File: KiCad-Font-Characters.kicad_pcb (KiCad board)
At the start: 2 copper layers, 296 x 287 mm, 0 parts

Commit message: Modified layout to one column and updated with Greek/Coptic and Cyrillic pages
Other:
- board size 296 x 287 mm -> 147 x 801 mm
- board text added: "KiCad Font - Unicode Pages not implemented are omitted"
- board text removed: "KiCad Font"
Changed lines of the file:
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@@
     (thickness 1.6)
   )
-  (paper "User" 315.011 315.011)
+  (paper "User" 167.005 821.004)
   (title_block
     (title "KiCad Font Characters")
@@
     )
     (pad_to_mask_clearance 0)
-    (grid_origin 13 14)
     (pcbplotparams
       (layerselection 0x0000020_7ffffffe)
@@
   )
   (net 0 "")
-  (gr_line (start 176 82) (end 176 136)
-    (stroke (width 0.15) (type default)) (layer "F.SilkS"))
-  (gr_line (start 176 150) (end 176 172)
-    (stroke (width 0.15) (type default)) (layer "F.SilkS"))
-  (gr_line (start 303 86) (end 162 86)
+  (gr_line (start 27 596) (end 27 650)
+    (stroke (width 0.15) (type default)) (layer "F.SilkS"))
+  (gr_line (start 27 664) (end 27 686)
+    (stroke (width 0.15) (type default)) (layer "F.SilkS"))
+  (gr_line (start 154 600) (end 13 600)
     (stroke (width 0.15) (type default)) (layer "F.SilkS"))
   (gr_line (start 27 139) (end 27 193)
     (stroke (width 0.15) (type default)) (layer "F.SilkS"))
-  (gr_line (start 162 31) (end 303 31)
-    (stroke (width 0.15) (type default)) (layer "F.SilkS"))
-  (gr_line (start 176 27) (end 176 68)
+  (gr_line (start 13 443) (end 154 443)
+    (stroke (width 0.15) (type default)) (layer "F.SilkS"))
+  (gr_line (start 13 313) (end 154 313)
+    (stroke (width 0.15) (type default)) (layer "F.SilkS"))
+  (gr_line (start 27 309) (end 27 350)
+    (stroke (width 0.15) (type default)) (layer "F.SilkS"))
+  (gr_line (start 13 564) (end 154 564)
     (stroke (width 0.15) (type default)) (layer "F.SilkS"))
   (gr_line (start 13 143) (end 154 143)
@@
   (gr_line (start 13 87) (end 154 87)
     (stroke (width 0.15) (type default)) (layer "F.SilkS"))
-  (gr_line (start 176 186) (end 176 285)
+  (gr_line (start 27 700) (end 27 799)
     (stroke (width 0.15) (type default)) (layer "F.SilkS"))
   (gr_line (start 27 27) (end 27 68)
     (stroke (width 0.15) (type default)) (layer "F.SilkS"))
-  (gr_line (start 303 154) (end 162 154)
+  (gr_line (start 27 560) (end 27 582)
+    (stroke (width 0.15) (type default)) (layer "F.SilkS"))
+  (gr_line (start 154 668) (end 13 668)
+    (stroke (width 0.15) (type default)) (layer "F.SilkS"))
+  (gr_line (start 13 368) (end 154 368)
     (stroke (width 0.15) (type default)) (layer "F.SilkS"))
   (gr_line (start 27 208) (end 27 294)
@@
   (gr_line (start 27 83) (end 27 124)
     (stroke (width 0.15) (type default)) (layer "F.SilkS"))
-  (gr_line (start 304 190) (end 163 190)
+  (gr_line (start 155 704) (end 14 704)
+    (stroke (width 0.15) (type default)) (layer "F.SilkS"))
+  (gr_line (start 27 364) (end 27 425)
     (stroke (width 0.15) (type default)) (layer "F.SilkS"))
   (gr_line (start 13 212) (end 154 212)
@@
   (gr_line (start 13 31) (end 154 31)
     (stroke (width 0.15) (type default)) (layer "F.SilkS"))
-  (gr_rect (start 10 10) (end 306 297)
+  (gr_line (start 27 439) (end 27 545)
+    (stroke (width 0.15) (type default)) (layer "F.SilkS"))
+  (gr_rect (start 10 10) (end 157 811)
     (stroke (width 0.1) (type default)) (fill none) (layer "Edge.Cuts"))
-  (gr_text "KiCad Font" (at 12 15) (layer "F.SilkS")
+  (gr_text "KiCad Font - Unicode Pages not implemented are omitted" (at 12 15) (layer "F.SilkS")
     (effects (font (size 3 3) (thickness 0.5) bold) (justify left bottom))
   )
   (gr_text_box "Superscripts and Subscripts\n\n		0	1	2	3	4	5	6	7	8	9	A	B	C	D	E	F\n\nU+207x	⁰	ⁱ			⁴	⁵	⁶	⁷	⁸	⁹	⁺	⁻	⁼	⁽	⁾	ⁿ\n\nU+208x	₀	₁	₂	₃	₄	₅	₆	₇	₈	₉	₊	₋	₌	₍	₎	\n\nU+209x	ₐ	ₑ	ₒ	ₓ	ₔ	ₕ	ₖ	ₗ	ₘ	ₙ	ₚ	ₛ	ₜ			"
-    (start 160 142) (end 304 173) (layer "F.SilkS")
+    (start 11 656) (end 155 687) (layer "F.SilkS")
       (effects (font (size 2 2) (thickness 0.3)) (justify left top))
   )
@@
   )
   (gr_text_box "IPA Extensions\n\n		0	1	2	3	4	5	6	7	8	9	A	B	C	D	E	F\n\nU+025x	ɐ	ɑ	ɒ	ɓ	ɔ	ɕ	ɖ	ɗ	ɘ	ə	ɚ	ɛ	ɜ	ɝ	ɞ	ɟ\n\nU+026x	ɠ	ɡ	ɢ	ɣ	ɤ	ɥ	ɦ	ɧ	ɨ	ɩ	ɪ	ɫ	ɬ	ɭ	ɮ	ɯ\n\nU+027x	ɰ	ɱ	ɲ	ɳ	ɴ	ɵ	ɶ	ɷ	ɸ	ɹ	ɺ	ɻ	ɼ	ɽ	ɾ	ɿ\n\nU+028x	ʀ	ʁ	ʂ	ʃ	ʄ	ʅ	ʆ	ʇ	ʈ	ʉ	ʊ	ʋ	ʌ	ʍ	ʎ	ʏ\n\nU+029x	ʐ	ʑ	ʒ	ʓ	ʔ	ʕ	ʖ	ʗ	ʘ	ʙ	ʚ	ʛ	ʜ	ʝ	ʞ	ʟ\n\nU+02Ax	ʠ	ʡ	ʢ	ʣ	ʤ	ʥ	ʦ	ʧ	ʨ	ʩ	ʪ	ʫ	ʬ	ʭ	ʮ	ʯ"
-    (start 160 19) (end 304 69) (layer "F.SilkS")
+    (start 11 301) (end 155 351) (layer "F.SilkS")
       (effects (font (size 2 2) (thickness 0.3)) (justify left top))
   )
@@
   )
   (gr_text_box "Halfwidth and Fullwidth Forms\n\n		0	1	2	3	4	5	6	7	8	9	A	B	C	D	E	F\n\nU+FF0x		！	＂	＃	＄	％	＆	＇	（	）	＊	＋	，	－	．	／\n\nU+FF1x	０	１	２	３	４	５	６	７	８	９	：	；	＜	＝	＞	？\n\nU+FF2x	＠	Ａ	Ｂ	Ｃ	Ｄ	Ｅ	Ｆ	Ｇ	Ｈ	Ｉ	Ｊ	Ｋ	Ｌ	Ｍ	Ｎ	Ｏ\n\nU+FF3x	Ｐ	Ｑ	Ｒ	Ｓ	Ｔ	Ｕ	Ｖ	Ｗ	Ｘ	Ｙ	Ｚ	［	＼	］	＾	＿\n\nU+FF4x	｀	ａ	ｂ	ｃ	ｄ	ｅ	ｆ	ｇ	ｈ	ｉ	ｊ	ｋ	ｌ	ｍ	ｎ	ｏ\n\nU+FF5x	ｐ	ｑ	ｒ	ｓ	ｔ	ｕ	ｖ	ｗ	ｘ	ｙ	ｚ	｛	｜	｝	～	｟\n\nU+FF6x	｠	｡	｢	｣	､	･	ｦ	ｧ	ｨ	ｩ	ｪ	ｫ	ｬ	ｭ	ｮ	ｯ\n\nU+FF7x	ｰ	ｱ	ｲ	ｳ	ｴ	ｵ	ｶ	ｷ	ｸ	ｹ	ｺ	ｻ	ｼ	ｽ	ｾ	ｿ\n\nU+FF8x	ﾀ	ﾁ	ﾂ	ﾃ	ﾄ	ﾅ	ﾆ	ﾇ	ﾈ	ﾉ	ﾊ	ﾋ	ﾌ	ﾍ	ﾎ	ﾏ\n\nU+FF9x	ﾐ	ﾑ	ﾒ	ﾓ	ﾔ	ﾕ	ﾖ	ﾗ	ﾘ	ﾙ	ﾚ	ﾛ	ﾜ	ﾝ	ﾞ	ﾟ\n\nU+FFAx	HF	ﾡ	ﾢ	ﾣ	ﾤ	ﾥ	ﾦ	ﾧ	ﾨ	ﾩ	ﾪ	ﾫ	ﾬ	ﾭ	ﾮ	ﾯ\n\nU+FFBx	ﾰ	ﾱ	ﾲ	ﾳ	ﾴ	ﾵ	ﾶ	ﾷ	ﾸ	ﾹ	ﾺ	ﾻ	ﾼ	ﾽ	ﾾ	\n\nU+FFCx			ￂ	ￃ	ￄ	ￅ	ￆ	ￇ			ￊ	ￋ	ￌ	ￍ	ￎ	ￏ\n\nU+FFDx			ￒ	ￓ	ￔ	ￕ	ￖ	ￗ			ￚ	ￛ	ￜ			\n\nU+FFEx	￠	￡	￢	￣	￤	￥	￦		￨	￩	￪	￫	￬	￭	￮	"
-    (start 161 178) (end 305 286) (layer "F.SilkS")
+    (start 12 692) (end 156 800) (layer "F.SilkS")
       (effects (font (size 2 2) (thickness 0.3)) (justify left top))
   )
   (gr_text_box "Phonetic Extensions\n\n		0	1	2	3	4	5	6	7	8	9	A	B	C	D	E	F\n\nU+1D0x	ᴀ	ᴁ	ᴂ	ᴃ	ᴄ	ᴅ	ᴆ	ᴇ	ᴈ	ᴉ	ᴊ	ᴋ	ᴌ	ᴍ	ᴎ	ᴏ\n\nU+1D1x	ᴐ	ᴑ	ᴒ	ᴓ	ᴔ	ᴕ	ᴖ	ᴗ	ᴘ	ᴙ	ᴚ	ᴛ	ᴜ	ᴝ	ᴞ	ᴟ\n\nU+1D2x	ᴠ	ᴡ	ᴢ	ᴣ	ᴤ	ᴥ	ᴦ	ᴧ	ᴨ	ᴩ	ᴪ	ᴫ	ᴬ	ᴭ	ᴮ	ᴯ\n\nU+1D3x	ᴰ	ᴱ	ᴲ	ᴳ	ᴴ	ᴵ	ᴶ	ᴷ	ᴸ	ᴹ	ᴺ	ᴻ	ᴼ	ᴽ	ᴾ	ᴿ\n\nU+1D4x	ᵀ	ᵁ	ᵂ	ᵃ	ᵄ	ᵅ	ᵆ	ᵇ	ᵈ	ᵉ	ᵊ	ᵋ	ᵌ	ᵍ	ᵎ	ᵏ\n\nU+1D5x	ᵐ	ᵑ	ᵒ	ᵓ	ᵔ	ᵕ	ᵖ	ᵗ	ᵘ	ᵙ	ᵚ	ᵛ	ᵜ	ᵝ	ᵞ	ᵟ\n\nU+1D6x	ᵠ	ᵡ	ᵢ	ᵣ	ᵤ	ᵥ	ᵦ	ᵧ	ᵨ	ᵩ	ᵪ	ᵫ	ᵬ	ᵭ	ᵮ	ᵯ\n\nU+1D7x	ᵰ	ᵱ	ᵲ	ᵳ	ᵴ	ᵵ	ᵶ	ᵷ	ᵸ	ᵹ	ᵺ	ᵻ	ᵼ	ᵽ	ᵾ	ᵿ"
-    (start 160 74) (end 304 137) (layer "F.SilkS")
+    (start 11 588) (end 155 651) (layer "F.SilkS")
       (effects (font (size 2 2) (thickness 0.3)) (justify left top))
   )
@@
       (effects (font (size 2 2) (thickness 0.3)) (justify left top))
   )
+  (gr_text_box "Cyrillic\n\n 		0	1	2	3	4	5	6	7	8	9	A	B	C	D	E	F\n\nU+040x	Ѐ	Ё	Ђ	Ѓ	Є	Ѕ	І	Ї	Ј	Љ	Њ	Ћ	Ќ	Ѝ	Ў	Џ\n\nU+041x	А	Б	В	Г	Д	Е	Ж	З	И	Й	К	Л	М	Н	О	П\n\nU+042x	Р	С	Т	У	Ф	Х	Ц	Ч	Ш	Щ	Ъ	Ы	Ь	Э	Ю	Я\n\nU+043x	а	б	в	г	д	е	ж	з	и	й	к	л	м	н	о	п\n\nU+044x	р	с	т	у	ф	х	ц	ч	ш	щ	ъ	ы	ь	э	ю	я\n\nU+045x	ѐ	ё	ђ	ѓ	є	ѕ	і	ї	ј	љ	њ	ћ	ќ	ѝ	ў	џ\n\nU+046x	Ѡ	ѡ	Ѣ	ѣ	Ѥ	ѥ	Ѧ	ѧ	Ѩ	ѩ	Ѫ	ѫ	Ѭ	ѭ	Ѯ	ѯ\n\nU+047x	Ѱ	ѱ	Ѳ	ѳ	Ѵ	ѵ	Ѷ	ѷ	Ѹ	ѹ	Ѻ	ѻ	Ѽ	ѽ	Ѿ	ѿ\n\nU+048x	Ҁ	ҁ	҂	◌҃	◌҄	◌҅	◌҆	◌҇	◌҈	◌҉	Ҋ	ҋ	Ҍ	ҍ	Ҏ	ҏ\n\nU+049x	Ґ	ґ	Ғ	ғ	Ҕ	ҕ	Җ	җ	Ҙ	ҙ	Қ	қ	Ҝ	ҝ	Ҟ	ҟ\n\nU+04Ax	Ҡ	ҡ	Ң	ң	Ҥ	ҥ	Ҧ	ҧ	Ҩ	ҩ	Ҫ	ҫ	Ҭ	ҭ	Ү	ү\n\nU+04Bx	Ұ	ұ	Ҳ	ҳ	Ҵ	ҵ	Ҷ	ҷ	Ҹ	ҹ	Һ	һ	Ҽ	ҽ	Ҿ	ҿ\n\nU+04Cx	Ӏ	Ӂ	ӂ	Ӄ	ӄ	Ӆ	ӆ	Ӈ	ӈ	Ӊ	ӊ	Ӌ	ӌ	Ӎ	ӎ	ӏ\n\nU+04Dx	Ӑ	ӑ	Ӓ	ӓ	Ӕ	ӕ	Ӗ	ӗ	Ә	ә	Ӛ	ӛ	Ӝ	ӝ	Ӟ	ӟ\n\nU+04Ex	Ӡ	ӡ	Ӣ	ӣ	Ӥ	ӥ	Ӧ	ӧ	Ө	ө	Ӫ	ӫ	Ӭ	ӭ	Ӯ	ӯ\n\nU+04Fx	Ӱ	ӱ	Ӳ	ӳ	Ӵ	ӵ	Ӷ	ӷ	Ӹ	ӹ	Ӻ	ӻ	Ӽ	ӽ	Ӿ	ӿ"
+    (start 11 431) (end 155 547) (layer "F.SilkS")
+      (effects (font (size 2 2) (thickness 0.3)) (justify left top))
+  )
   (gr_text_box "Latin Extended-A\n\n		0	1	2	3	4	5	6	7	8	9	A	B	C	D	E	F\n\nU+010x	Ā	ā	Ă	ă	Ą	ą	Ć	ć	Ĉ	ĉ	Ċ	ċ	Č	č	Ď	ď\n\nU+011x	Đ	đ	Ē	ē	Ĕ	ĕ	Ė	ė	Ę	ę	Ě	ě	Ĝ	ĝ	Ğ	ğ\n\nU+012x	Ġ	ġ	Ģ	ģ	Ĥ	ĥ	Ħ	ħ	Ĩ	ĩ	Ī	ī	Ĭ	ĭ	Į	į\n\nU+013x	İ	ı	Ĳ	ĳ	Ĵ	ĵ	Ķ	ķ	ĸ	Ĺ	ĺ	Ļ	ļ	Ľ	ľ	Ŀ\n\nU+014x	ŀ	Ł	ł	Ń	ń	Ņ	ņ	Ň	ň	ŉ	Ŋ	ŋ	Ō	ō	Ŏ	ŏ\n\nU+015x	Ő	ő	Œ	œ	Ŕ	ŕ	Ŗ	ŗ	Ř	ř	Ś	ś	Ŝ	ŝ	Ş	ş\n\nU+016x	Š	š	Ţ	ţ	Ť	ť	Ŧ	ŧ	Ũ	ũ	Ū	ū	Ŭ	ŭ	Ů	ů\n\nU+017x	Ű	ű	Ų	ų	Ŵ	ŵ	Ŷ	ŷ	Ÿ	Ź	ź	Ż	ż	Ž	ž	ſ"
     (start 11 131) (end 156 195) (layer "F.SilkS")
+      (effects (font (size 2 2) (thickness 0.3)) (justify left top))
+  )
+  (gr_text_box "Greek and Coptic\n\n 		0	1	2	3	4	5	6	7	8	9	A	B	C	D	E	F\n\nU+037x	Ͱ	ͱ	Ͳ	ͳ	ʹ	͵	Ͷ	ͷ			ͺ	ͻ	ͼ	ͽ	;	Ϳ\n\nU+038x					΄	΅	Ά	·	Έ	Ή	Ί		Ό		Ύ	Ώ\n\nU+039x	ΐ	Α	Β	Γ	Δ	Ε	Ζ	Η	Θ	Ι	Κ	Λ	Μ	Ν	Ξ	Ο\n\nU+03Ax	Π	Ρ		Σ	Τ	Υ	Φ	Χ	Ψ	Ω	Ϊ	Ϋ	ά	έ	ή	ί\n\nU+03Bx	ΰ	α	β	γ	δ	ε	ζ	η	θ	ι	κ	λ	μ	ν	ξ	ο\n\nU+03Cx	π	ρ	ς	σ	τ	υ	φ	χ	ψ	ω	ϊ	ϋ	ό	ύ	ώ	Ϗ\n\nU+03Dx	ϐ	ϑ	ϒ	ϓ	ϔ	ϕ	ϖ	ϗ	Ϙ	ϙ	Ϛ	ϛ	Ϝ	ϝ	Ϟ	ϟ\n\nU+03Ex	Ϡ	ϡ	Ϣ	ϣ	Ϥ	ϥ	Ϧ	ϧ	Ϩ	ϩ	Ϫ	ϫ	Ϭ	ϭ	Ϯ	ϯ\n\nU+03Fx	ϰ	ϱ	ϲ	ϳ	ϴ	ϵ	϶	Ϸ	ϸ	Ϲ	Ϻ	ϻ	ϼ	Ͻ	Ͼ	Ͽ"
+    (start 11 356) (end 155 426) (layer "F.SilkS")
+      (effects (font (size 2 2) (thickness 0.3)) (justify left top))
+  )
+  (gr_text_box "Cyrillic Supplement\n\n 		0	1	2	3	4	5	6	7	8	9	A	B	C	D	E	F\n\nU+050x	Ԁ	ԁ	Ԃ	ԃ	Ԅ	ԅ	Ԇ	ԇ	Ԉ	ԉ	Ԋ	ԋ	Ԍ	ԍ	Ԏ	ԏ\n\nU+051x	Ԑ	ԑ	Ԓ	ԓ	Ԕ	ԕ	Ԗ	ԗ	Ԙ	ԙ	Ԛ	ԛ	Ԝ	ԝ	Ԟ	ԟ\n\nU+052x	Ԡ	ԡ	Ԣ	ԣ	Ԥ	ԥ	Ԧ	ԧ	Ԩ	ԩ	Ԫ	ԫ	Ԭ	ԭ	Ԯ	ԯ"
+    (start 11 552) (end 155 583) (layer "F.SilkS")
       (effects (font (size 2 2) (thickness 0.3)) (justify left top))
   )
@@
     )
   )
+  (group "" (id 77080d20-7dbb-40e9-8009-72fe85131f03)
+    (members
+      5534f6d2-ff0e-4ebf-ba5c-00a53f904439
+      84d42f44-7b8b-4db7-ad40-aab2f311ec1e
+      d20204fd-e319-4ef5-9a35-a9e0c8180bc3
+    )
+  )
+  (group "" (id 7e93d43a-a84d-4ec8-91a4-9e577e1dfa8f)
+    (members
+      a5bdbdbb-49a0-4e5f-9317-b53eed74a0f1
+      c64d20d1-3817-40d7-908a-75a97b4ecf2a
+      de2a1a59-7cbb-4870-a01e-319e80d73d3f
+    )
+  )
   (group "" (id 981cf8f1-002d-401e-a745-66a3b6efa2e8)
     (members
@@
     )
   )
+  (group "" (id f8b6e90c-8303-4a87-a758-f86a4a62b125)
+    (members
+      2a98ef6d-016e-49c6-9505-a908858d9f8e
+      ad96964a-7ff5-4070-9d4b-ed82cc239925
+      f1458d6d-a49b-499c-aad6-274b759a0b69
+    )
+  )

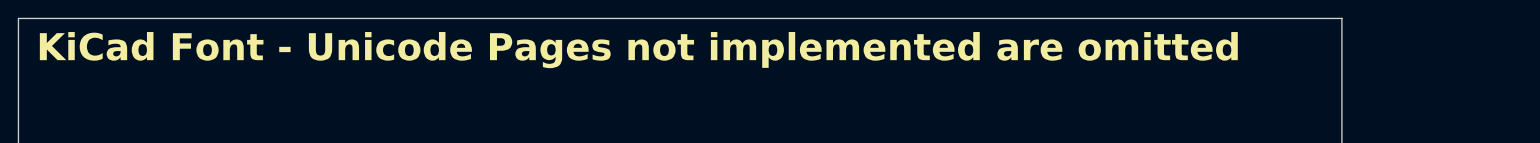
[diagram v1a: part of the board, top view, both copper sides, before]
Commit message: Unicode "Pages" -> "Blocks"
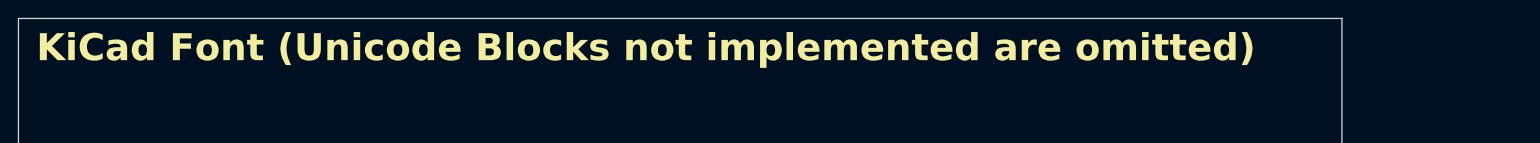
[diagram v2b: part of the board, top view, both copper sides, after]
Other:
- board text added: "KiCad Font (Unicode Blocks not implemented are omitted)"
- board text removed: "KiCad Font - Unicode Pages not implemented are omitted"
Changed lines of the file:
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@@
       (sketchpadsonfab false)
       (subtractmaskfromsilk false)
-      (outputformat 5)
+      (outputformat 4)
       (mirror false)
       (drillshape 0)
@@
   (gr_rect (start 10 10) (end 157 811)
     (stroke (width 0.1) (type default)) (fill none) (layer "Edge.Cuts"))
-  (gr_text "KiCad Font - Unicode Pages not implemented are omitted" (at 12 15) (layer "F.SilkS")
+  (gr_text "KiCad Font (Unicode Blocks not implemented are omitted)" (at 12 15) (layer "F.SilkS")
     (effects (font (size 3 3) (thickness 0.5) bold) (justify left bottom))
   )

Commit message: Added further Unicode Blocks and reordering
Table formatted in three columns, grouped by Script
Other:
- board size 147 x 801 mm -> 453 x 498 mm
- board text added: "Common"
- board text added: "Coptic"
- board text added: "Cyrillic"
- board text added: "Greek"
- board text added: "KiCad Font - Unicode Blocks"
- board text added: "Latin"
- board text added: "Unimplemented Blocks are omitted Grouped by Writing System (Script)"
- board text removed: "KiCad Font (Unicode Blocks not implemented are omitted)"
